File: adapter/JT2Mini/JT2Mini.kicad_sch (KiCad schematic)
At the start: 5 parts, among them J1 CBE224, J2 3220-10-0300-00

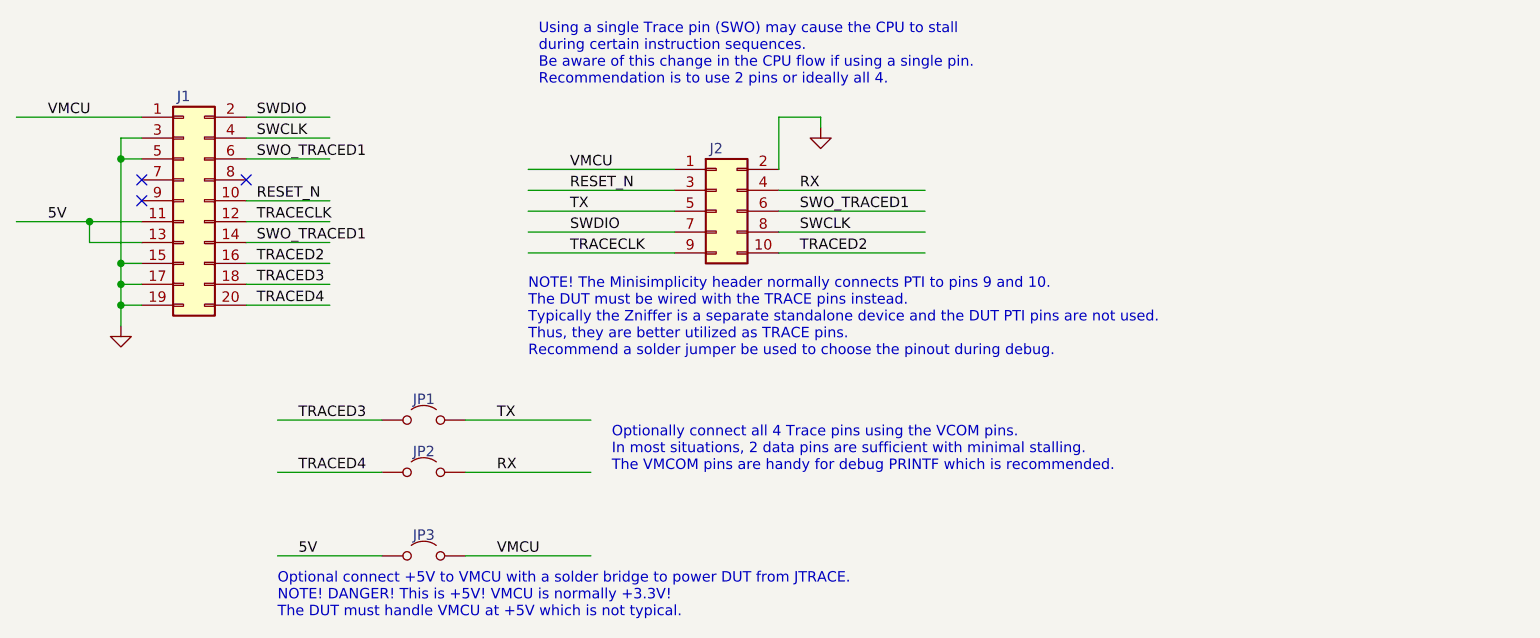
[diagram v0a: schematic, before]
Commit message: Rev B PCB - added test points and GND for checking signal integrity
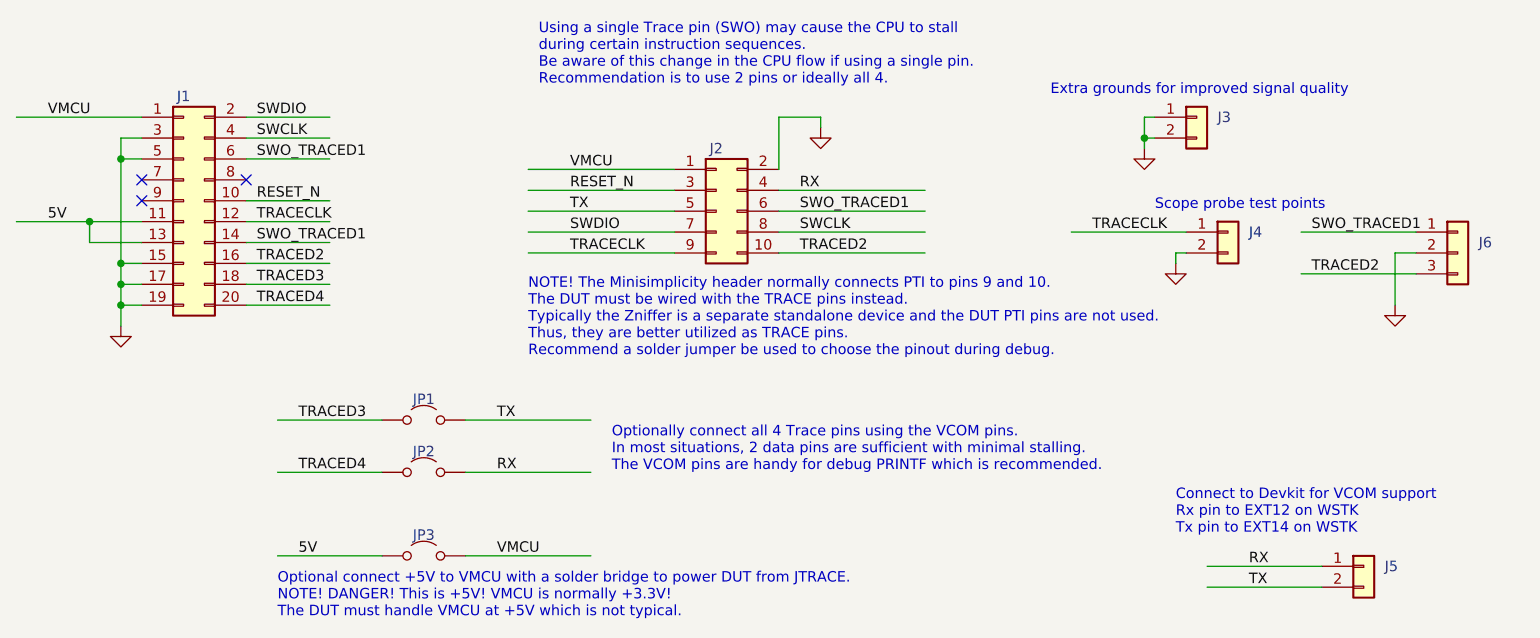
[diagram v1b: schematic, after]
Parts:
- added J3, J4, J5: Conn_01x02, Connector_PinHeader_2.54mm:PinHeader_1x02_P2.54mm_Vertical, symbol Connector_Generic:Conn_01x02
- added J6: Conn_01x03, Connector_PinHeader_2.54mm:PinHeader_1x03_P2.54mm_Vertical, symbol Connector_Generic:Conn_01x03
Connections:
- net GND: now also J3.1 (Pin_1), J3.2 (Pin_2), J4.2 (Pin_2), J6.2 (Pin_2)
- net RX: now also J5.1 (Pin_1)
- net SWO_TRACED1: now also J6.1 (Pin_1)
- net TRACECLK: now also J4.1 (Pin_1)
- net TRACED2: now also J6.3 (Pin_3)
- net TX: now also J5.2 (Pin_2)
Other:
- note added: "Connect to Devkit for VCOM support Rx pin to EXT12 on WSTK Tx pin to EXT14 on WSTK"
- note added: "Extra grounds for improved signal quality"
- note added: "Optionally connect all 4 Trace pins using the VCOM pins. In most situations, 2 data pins are sufficient with minimal stalling. The VCOM pins are handy for debug PRINTF which is recommended."
- note added: "Scope probe test points"
- note removed: "Optionally connect all 4 Trace pins using the VCOM pins. In most situations, 2 data pins are sufficient with minimal stalling. The VMCOM pins are handy for debug PRINTF which is recommended."
